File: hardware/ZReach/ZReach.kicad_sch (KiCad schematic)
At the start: 2 parts, among them J1 USB_C_Receptacle, U1 CP2102N-Axx-xQFN20

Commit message: Initial schematic and Tech Doc checkin
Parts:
- removed J1: USB_C_Receptacle, symbol Connector:USB_C_Receptacle
- added C1: C_Small, Capacitor_SMD:C_0603_1608Metric, symbol Device:C_Small
- added C10, C13: 1UF, Capacitor_SMD:C_0603_1608Metric, symbol Device:C_Small
- added C11, C12: 220P, Capacitor_SMD:C_0603_1608Metric, symbol Device:C_Small
- added C2: 1P9, Capacitor_SMD:C_0402_1005Metric, symbol Device:C_Small
- added C3: 220P, Capacitor_SMD:C_0402_1005Metric, symbol Device:C_Small
- added C4: 47P, Capacitor_SMD:C_0402_1005Metric, symbol Device:C_Small
- added C5, C6: NM, Capacitor_SMD:C_0402_1005Metric, symbol Device:C_Small
- added C7: 7P2, Capacitor_SMD:C_0402_1005Metric, symbol Device:C_Small
- added C8: 1P3, Capacitor_SMD:C_0402_1005Metric, symbol Device:C_Small
- added C9: 4U7, Capacitor_SMD:C_0805_2012Metric, symbol Device:C_Small
- added J1: USB_C_Receptacle_USB2.0, symbol Connector:USB_C_Receptacle_USB2.0
- added J2: Conn_02x05_Odd_Even, Connector:Tag-Connect_TC2050-IDC-NL_2x05_P1.27mm_Vertical, symbol Connector_Generic:Conn_02x05_Odd_Even
- added J3: SMA, Connector_Coaxial:SMA_Wurth_60312002114503_Vertical, symbol Connector:Conn_Coaxial
- added J4: NM, Connector_Coaxial:U.FL_Hirose_U.FL-R-SMT-1_Vertical, symbol Connector:Conn_Coaxial
- added J5: Conn_01x04, symbol Connector_Generic:Conn_01x04
- added L1: 18N, Inductor_SMD:L_0402_1005Metric, symbol Device:L_Small
- added L2: 1N5, Inductor_SMD:L_0402_1005Metric, symbol Device:L_Small
- added L3: 1N3, Inductor_SMD:L_0402_1005Metric, symbol Device:L_Small
- added L4: 13N, Inductor_SMD:L_0402_1005Metric, symbol Device:L_Small
- added L5: 2U2, Inductor_SMD:L_0603_1608Metric, symbol Device:L_Small
- added L6, L7, L8: 33@100, Inductor_SMD:L_0603_1608Metric, symbol Device:L_Ferrite_Small
- added R1, R2: 5K1, Resistor_SMD:R_0201_0603Metric, symbol Device:R_US
- added SW1: PTS810, Button_Switch_SMD:SW_SPST_PTS810, symbol Switch:SW_Push
- added U2: EFR32xG23-QFN48, Package_DFN_QFN:VQFN-48-1EP_6x6mm_P0.4mm_EP4.1x4.1mm, symbol MCU_Silabs:EFR32xG23-QFN48
- added U3: AP2127K-3.3, Package_TO_SOT_SMD:SOT-23-5, symbol Regulator_Linear:AP2127K-3.3
- added Y1: 39MHz 10ppm, symbol Device:Crystal_GND24
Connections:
- net DPLUS: now reaches U1.4 (D+)
- net DPLUS: now also J1.A6 (D+), J1.B6 (D+)
- net DMINUS: now reaches U1.5 (D-)
- net DMINUS: now also J1.A7 (D-), J1.B7 (D-)
- net VBUS_5V: now reaches U1.8 (VBUS)
- net VBUS_5V: now also J1.A4 (VBUS), J1.A9 (VBUS), J1.B4 (VBUS), J1.B9 (VBUS), U3.1 (VIN), U3.3 (EN)
- new net: U2.12 (HFXO), Y1.1
- new net: U2.11 (HFXI), Y1.3
- new net: C12.2, L8.2, U2.20 (PAVDD)
- new net: J1.A5 (CC1), R1.1
- new net: J1.B5 (CC2), R2.1
- new net: J1.S1 (SHIELD), L7.1
- new net: L5.1, U2.37 (VREGSW)
- new net: C3.1, C8.1, L4.2
- new net: C11.1, L6.2, U2.14 (RFVDD)
- new net: C1.1, U2.36 (DECOUPLE)
- new net: C2.2, L2.2, L3.1
- new net +1V8: C10.2, C9.2, L5.2, L6.1, U2.40 (DVDD)
- new net +3.3V: C13.2, L8.1, U2.38 (VREGVDD), U2.41 (AVDD), U2.42 (IOVDD), U3.5 (VOUT)
- new net GND: C1.2, C10.1, C11.2, C12.1, C13.1, C5.1, C6.1, C7.2, C8.2, C9.1, J1.A1 (GND), J1.A12 (GND), J1.B1 (GND), J1.B12 (GND), J2.2 (Pin_2), J3.2 (Ext), J4.2 (Ext), L7.2, R1.2, R2.2, SW1.1, U2.15 (RFVSS), U2.39 (VREGVSS), U2.49 (PAD), U3.2 (GND), Y1.2, Y1.4
- new net LED_BLUE: U2.5 (PC04)
- new net LED_GREEN: U2.25 (PA00)
- new net LED_RED: U2.23 (PB01)
- new net RF: C4.2, C6.2, J3.1 (In)
- new net RF50: C3.2, C4.1, C5.2, J4.1 (In), L1.2
- new net RFRX: L1.1, U2.17 (SUBGI0)
- new net RFTX1: C2.1, L2.1, U2.19 (SUBGO0)
- new net RFTX3: C7.1, L3.2, L4.1
- new net SWCLK: J2.8 (Pin_8), U2.26 (PA01_SWCLK)
- new net SWDIO: J2.7 (Pin_7), U2.27 (PA02_SWDIO)
- new net SWO: J2.6 (Pin_6), U2.28 (PA03_SWO)
- new net TCLK: J2.10 (Pin_10), U2.30 (PA05_TD1)
- new net TD1: J2.9 (Pin_9), U2.29 (PA04_TCLK)
- new net VCOMRX: J2.4 (Pin_4), U2.34 (PA09_URX)
- new net VCOMTX: J2.5 (Pin_5), U2.33 (PA08_UTX)
- new net ~{LEARN}: SW1.2, U2.6 (PC05)
- new net ~{RESET}: J2.3 (Pin_3), U2.13 (~{RESET})
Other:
- note added: "50 OHM MATCH & FILTER"
- note added: "ANTENNA TUNE VALUES DETERMINED AFTER TUNING"
- note added: "QWIIC"
- note added: "Silabs Minisimplicity Tag-Connect 10 pin Debug Header"
- note added: "Two Bits of Trace debug PTI is not used"
- note added: "UFL for tuning"
- moved on the sheet: U1

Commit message: started ERC checking
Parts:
- removed J5: Conn_01x04, symbol Connector_Generic:Conn_01x04
- added C14, C16, C17: 100N, Capacitor_SMD:C_0603_1608Metric, symbol Device:C_Small
- added C15, C18, C19: 4U7, Capacitor_SMD:C_0805_2012Metric, symbol Device:C_Small
- added D1: SP0503BAHT, Package_TO_SOT_SMD:SOT-143, symbol Power_Protection:SP0503BAHT
- added D2: LED_BGRK, symbol Device:LED_BGRK
- added J5: Qwiic_RA, ZReach:JST_PTH-4, symbol ZReach:Qwiic_Right_Angle
- added R3, R4: 100, Resistor_SMD:R_0603_1608Metric, symbol Device:R_US
- added R5: 22K1, Resistor_SMD:R_0603_1608Metric, symbol Device:R_US
- added R6: 47K5, Resistor_SMD:R_0603_1608Metric, symbol Device:R_US
- added R7: 1K2, Resistor_SMD:R_0603_1608Metric, symbol Device:R_US
- added R8: 1K, Resistor_SMD:R_0603_1608Metric, symbol Device:R_US
- added R9: 820, Resistor_SMD:R_0603_1608Metric, symbol Device:R_US
- added Y2: 32768Hz, symbol Device:Crystal
- C1: value C_Small -> 1UF
- R1, R2: footprint Resistor_SMD:R_0201_0603Metric -> Resistor_SMD:R_0603_1608Metric
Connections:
- net +3.3V: now also J2.1 (Pin_1), C14.2, C15.2, D2.4 (K)
- net DECOUPLE: now also C1.1, U2.36 (DECOUPLE)
- net DMINUS: now also D1.3 (K)
- net DPLUS: now also D1.2 (K)
- net GND: now also U1.12 (GND), U1.21 (GND), U1.3 (GND), C14.1, C15.1, C16.1, C17.1, C18.1, C19.1, D1.1 (A), R6.1
- net LED_BLUE: now also R9.2
- net LED_GREEN: now also R8.2
- net LED_RED: now also R7.2
- net RFTX2: now also C2.2, L2.2, L3.1
- net RFTX4: now also C3.1, C8.1, L4.2
- net VBUS_5V: now also U1.7 (VREGIN), C17.2, C19.2, D1.4 (K), R5.1; no longer U1.8 (VBUS)
- net VCOMRX: now also R4.2
- net VCOMTX: now also R3.2
- net VREGSW: now also L5.1, U2.37 (VREGSW)
- net at U2.47 (PD01_LFXI): now also Y2.2
- net at U2.48 (PD00_LFXO): now also Y2.1
- net at U1.17 (RXD): now also R4.1
- net at U1.18 (TXD): now also R3.1
- net at U1.6 (VDD): now also U1.9 (~{RST}), C16.2, C18.2
- new net: D2.3 (RA), R7.1
- new net: D2.1 (BA), R9.1
- new net: D2.2 (GA), R8.1
- new net: R5.2, R6.2, U1.8 (VBUS)
- new net: J5.NC1 (NC), J5.NC2 (NC)
- no-connect marks 0 -> 17
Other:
- note added: "Optional RTC Crystal for Time CC End Devices"
- note added: "RGB Status LED NM for controller"
- note added: "Two Bits of Trace debug. PTI is not used. WSTK pwr slide switch MUST be in SELF."
- note removed: "Two Bits of Trace debug PTI is not used"
- moved on the sheet: C1, C12, C13, L5, L8, U1, U3, Y1

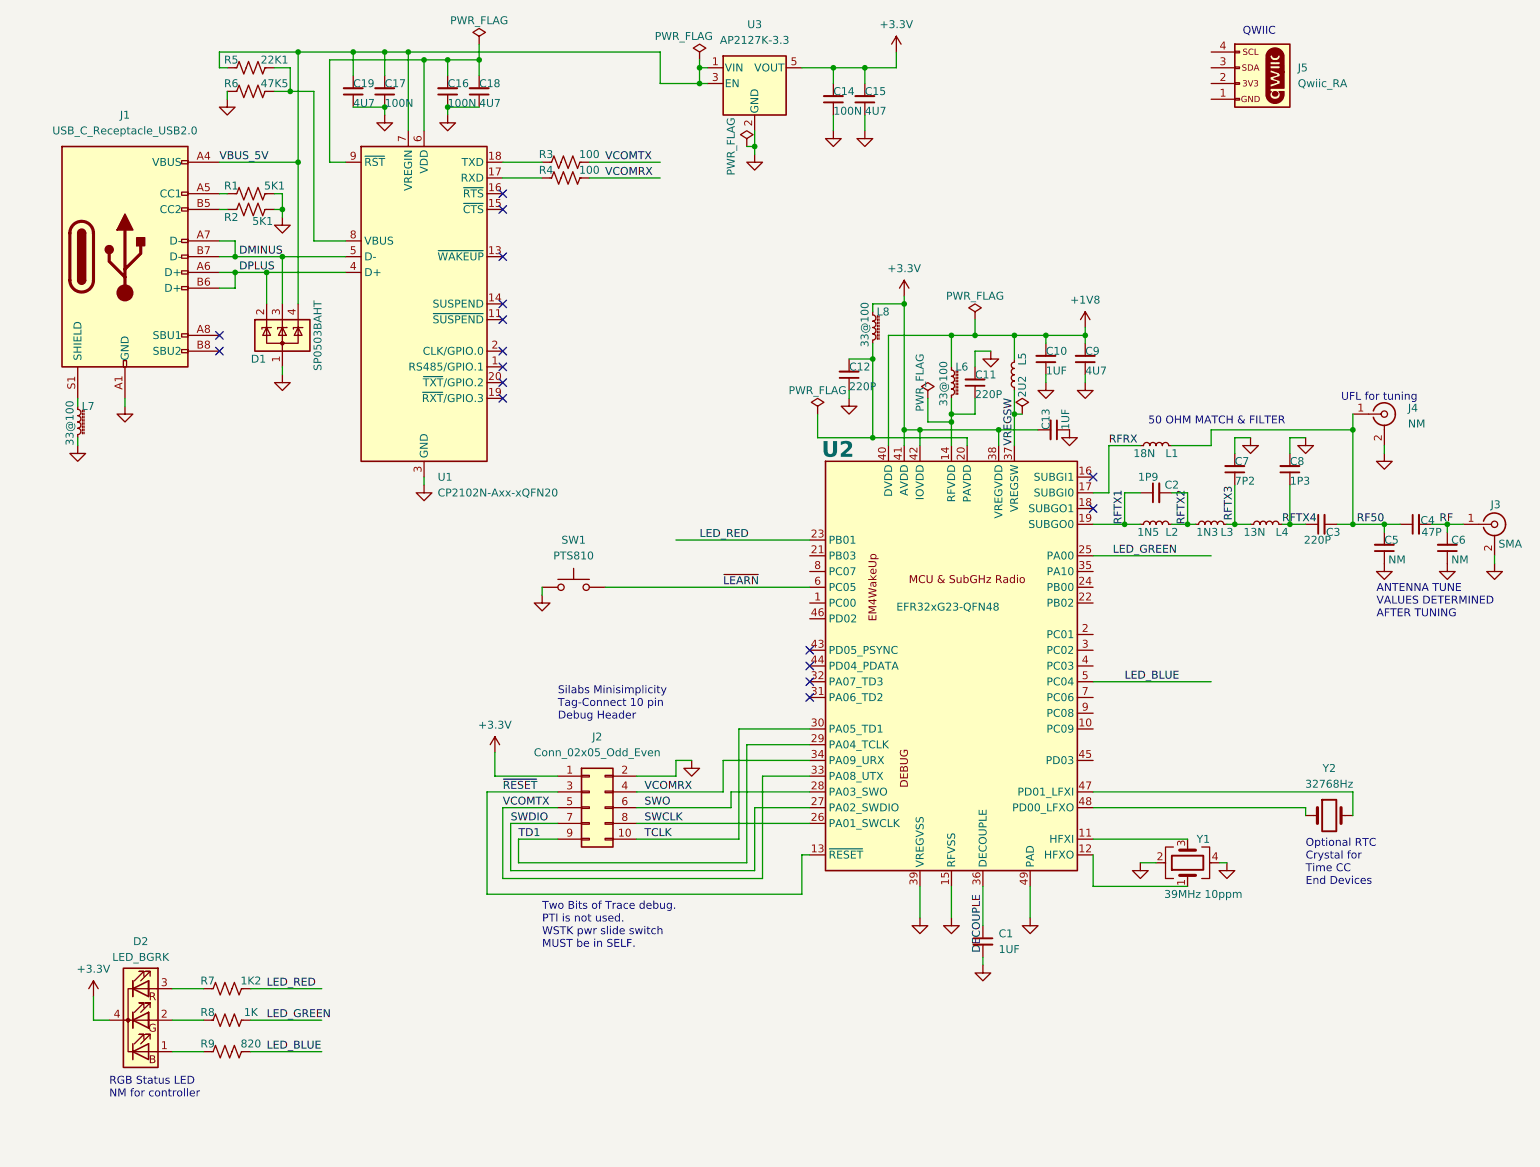
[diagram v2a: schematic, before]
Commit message: Schematic complete. PCB started.
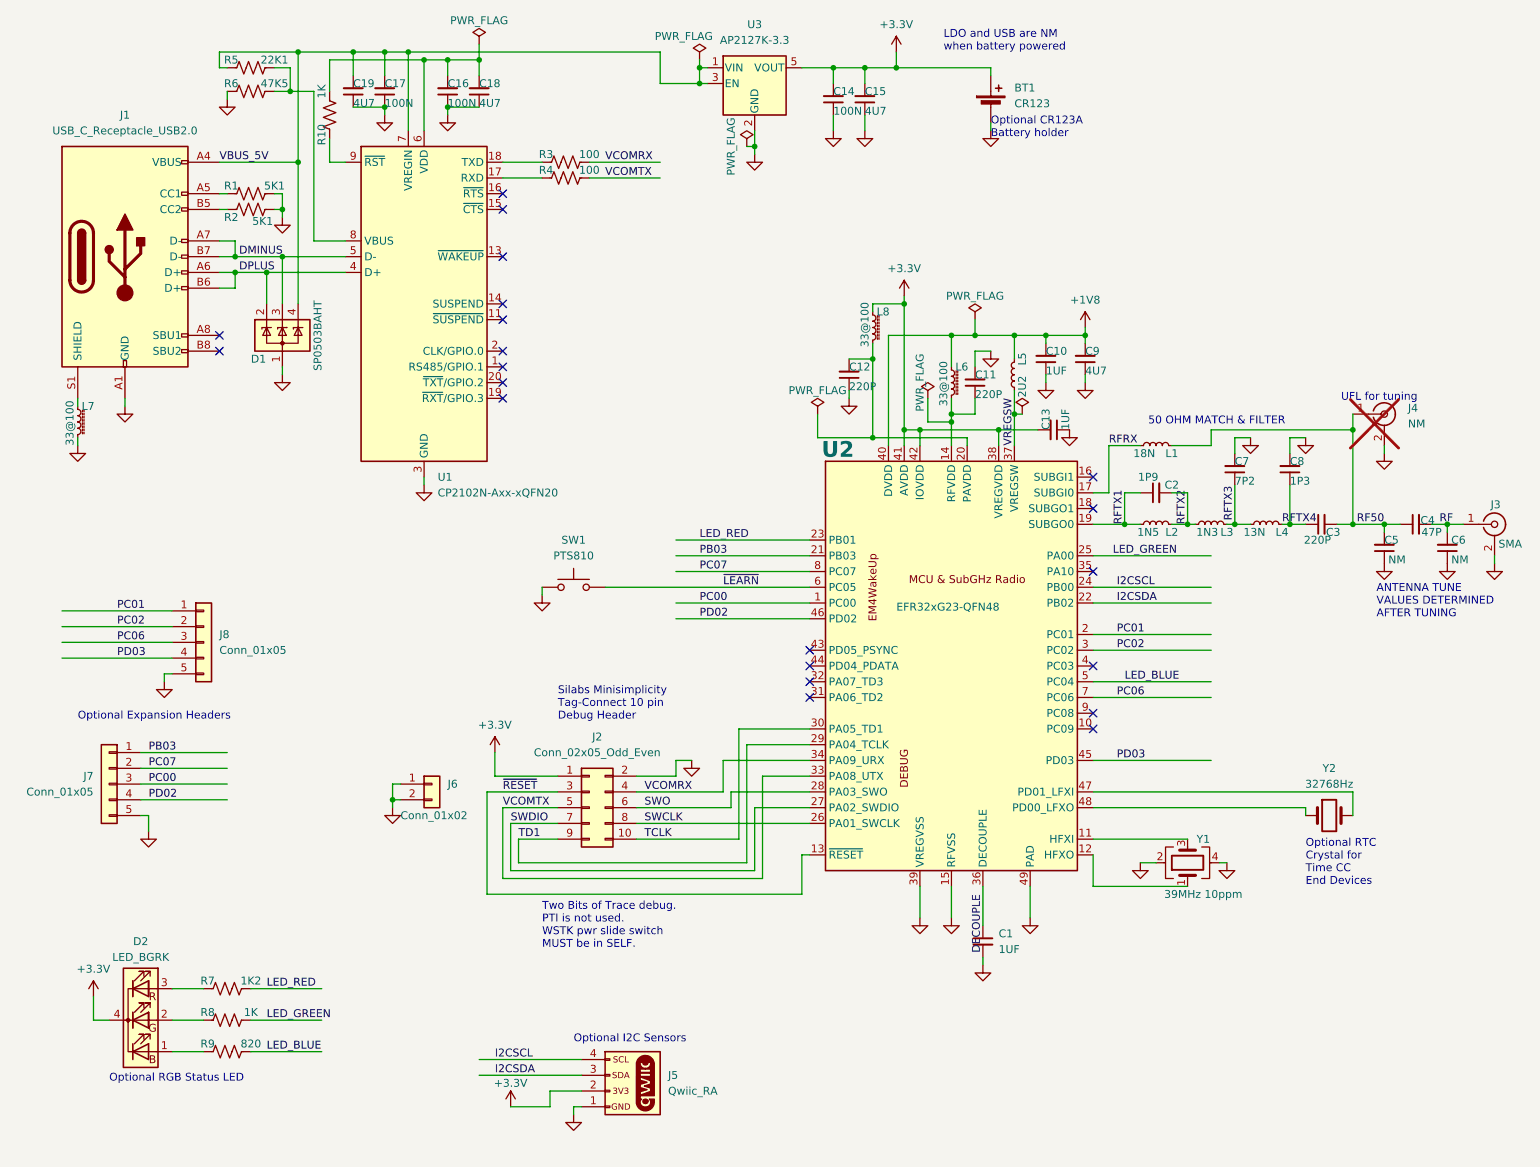
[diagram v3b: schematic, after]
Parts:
- added BT1: CR123, ZReach:1050_KEY, symbol Device:Battery_Cell
- added J6: Conn_01x02, Connector_PinHeader_2.54mm:PinHeader_1x02_P2.54mm_Vertical, symbol Connector_Generic:Conn_01x02
- added J7, J8: Conn_01x05, Connector_PinHeader_2.54mm:PinHeader_1x05_P2.54mm_Vertical, symbol Connector_Generic:Conn_01x05
- added R10: 1K, Resistor_SMD:R_0603_1608Metric, symbol Device:R_US
- D2: footprint (none) -> LED_SMD:LED_WS2812B-2020_PLCC4_2.0x2.0mm
- J1: footprint (none) -> Connector_USB:USB_C_Receptacle_GCT_USB4110
- J4: now not fitted; now left out of the parts list
- U1: footprint Package_DFN_QFN:SiliconLabs_QFN-20-1EP_3x3mm_P0.5mm -> Package_DFN_QFN:SiliconLabs_QFN-20-1EP_3x3mm_P0.5mm_EP1.8x1.8mm
- Y1: footprint (none) -> Crystal:Crystal_SMD_3225-4Pin_3.2x2.5mm
- Y2: footprint (none) -> Crystal:Crystal_SMD_3215-2Pin_3.2x1.5mm
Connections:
- net +3.3V: now also J5.2 (Pin_2), BT1.1 (+)
- net GND: now also J5.1 (Pin_1), BT1.2 (-), J6.1 (Pin_1), J6.2 (Pin_2), J7.5 (Pin_5), J8.5 (Pin_5)
- net VCOMRX: now also R3.2; no longer R4.2
- net VCOMTX: now also R4.2; no longer R3.2
- net PC00: now reaches U2.1 (PC00)
- net PC00: now also J7.3 (Pin_3)
- net PC01: now reaches U2.2 (PC01)
- net PC01: now also J8.1 (Pin_1)
- net PB03: now reaches U2.21 (PB03)
- net PB03: now also J7.1 (Pin_1)
- net I2CSDA: now reaches U2.22 (PB02)
- net I2CSDA: now also J5.3 (Pin_3)
- net I2CSCL: now reaches U2.24 (PB00)
- net I2CSCL: now also J5.4 (Pin_4)
- net PC02: now reaches U2.3 (PC02)
- net PC02: now also J8.2 (Pin_2)
- net PD03: now reaches U2.45 (PD03)
- net PD03: now also J8.4 (Pin_4)
- net PD02: now reaches U2.46 (PD02)
- net PD02: now also J7.4 (Pin_4)
- net PC06: now reaches U2.7 (PC06)
- net PC06: now also J8.3 (Pin_3)
- net PC07: now reaches U2.8 (PC07)
- net PC07: now also J7.2 (Pin_2)
- net at C16.2, C18.2, U1.6 (VDD): now also R10.2; no longer U1.9 (~{RST})
- new net: R10.1, U1.9 (~{RST})
- no-connect marks 17 -> 21
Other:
- note added: "LDO and USB are NM when battery powered"
- note added: "Optional CR123A Battery holder"
- note added: "Optional Expansion Headers"
- note added: "Optional I2C Sensors"
- note added: "Optional RGB Status LED"
- note removed: "QWIIC"
- note removed: "RGB Status LED NM for controller"
- moved on the sheet: J5
